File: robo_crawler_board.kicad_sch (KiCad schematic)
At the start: 24 parts, among them J1 Screw_Terminal_01x02, J2 Screw_Terminal_01x02, J3 Screw_Terminal_01x02, J4 Screw_Terminal_01x02, J5 Screw_Terminal_01x02, J6 Screw_Terminal_01x02, J7 Screw_Terminal_01x02, J8 Screw_Terminal_01x02, J9 Screw_Terminal_01x02, Q1 IRLZ44N, Q2 IRLZ44N, U1 DRV8871DDA, U2 DRV8871DDA, U3 DRV8871DDA, U4 DRV8871DDA, U8 DRV8871DDA, U9 DRV8871DDA

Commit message: cleaning repo
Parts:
- added R1, R2, R3, R4, R5, R6: 15k, Resistor_SMD:R_0805_2012Metric, symbol Device:R
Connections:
- net GND: now also R1.2, R2.2, R3.2, R4.2, R5.2, R6.2
- net at U1.4 (ILIM): now also R1.1
- net at U2.4 (ILIM): now also R2.1
- net at U4.4 (ILIM): now also R4.1
- net at U3.4 (ILIM): now also R3.1
- net at U9.4 (ILIM): now also R6.1
- net at U8.4 (ILIM): now also R5.1

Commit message: Reworking board design
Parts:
- removed J1, J2: Screw_Terminal_01x02, TerminalBlock:TerminalBlock_bornier-2_P5.08mm, symbol Connector:Screw_Terminal_01x02
- removed Q1, Q2: IRLZ44N, Package_TO_SOT_THT:TO-220-3_Vertical, symbol Transistor_FET:IRLZ44N
- removed U2, U3, U4: DRV8871DDA, Package_SO:Texas_HTSOP-8-1EP_3.9x4.9mm_P1.27mm_EP2.95x4.9mm_Mask2.4x3.1mm_ThermalVias, symbol Driver_Motor:DRV8871DDA
- added U5, U6, U7: DRV8871DDA, Package_SO:Texas_HTSOP-8-1EP_3.9x4.9mm_P1.27mm_EP2.95x4.9mm_Mask2.4x3.1mm_ThermalVias, symbol Driver_Motor:DRV8871DDA
- H1, H2, H3, H4: footprint MountingHole:MountingHole_2.2mm_M2 -> MountingHole:MountingHole_2.2mm_M2_Pad; symbol Mechanical:MountingHole -> Mechanical:MountingHole_Pad
- U2: renamed from U6; Part Name (none) -> LM2596 BC dev board
- renumbered J9 to J1, J8 to J2, U5 to U1, U7 to U3, U1 to U4
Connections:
- net +12V: now also U2.4 (OUT+), U5.5 (VM), U6.5 (VM), U7.5 (VM); no longer U3.4 (OUT+)
- net +5V: now also U3.4 (OUT+); no longer U2.4 (OUT+)
- net GND: now also H1.1, H2.1, H3.1, H4.1, U1.38 (GND), U5.1 (GND), U5.7 (GND), U5.9 (GND), U6.1 (GND), U6.7 (GND), U6.9 (GND), U7.1 (GND), U7.7 (GND), U7.9 (GND); no longer J1.1 (Pin_1), U1.15 (GND), U2.1 (IN-), U3.1 (IN-)
- net MOTOR1_CH2: now reaches U4.2 (IN2)
- net MOTOR1_CH2: now also U1.16 (IO13); no longer U1.12 (IO27)
- net MOTOR1_CH1: now reaches U4.3 (IN1)
- net MOTOR1_CH1: now also U1.14 (IO12); no longer U1.11 (IO26)
- net at J5.1 (Pin_1): now also U7.6 (OUT1)
- net at J5.2 (Pin_2): now also U7.8 (OUT2)
- net at J7.1 (Pin_1): now also U9.6 (OUT1)
- net at J7.2 (Pin_2): now also U9.8 (OUT2)
- net MOTOR5_CH2: now reaches U1.37 (IO23)
- net MOTOR5_CH2: now also U8.2 (IN2)
- net MOTOR5_CH1: now reaches U1.36 (IO22)
- net MOTOR5_CH1: now also U8.3 (IN1)
- net at R2.1: now also U5.4 (ILIM)
- net MOTOR2_CH1: now reaches U1.13 (IO14)
- net MOTOR2_CH1: now also U5.3 (IN1)
- net MOTOR2_CH2: now reaches U1.25 (IO0)
- net MOTOR2_CH2: now also U5.2 (IN2)
- net MOTOR3_CH1: now reaches U1.27 (IO16)
- net MOTOR3_CH1: now also U6.3 (IN1); no longer U9.3 (IN1)
- net MOTOR3_CH2: now reaches U1.28 (IO17)
- net MOTOR3_CH2: now also U6.2 (IN2); no longer U9.2 (IN2)
- net MOTOR4_CH1: now reaches U1.30 (IO18)
- net MOTOR4_CH1: now also U7.3 (IN1); no longer U8.3 (IN1)
- net MOTOR4_CH2: now reaches U1.31 (IO19)
- net MOTOR4_CH2: now also U7.2 (IN2); no longer U8.2 (IN2)
- net at R4.1: now also U7.4 (ILIM)
- net at J4.1 (Pin_1): now also U6.6 (OUT1); no longer U9.6 (OUT1)
- net at J4.2 (Pin_2): now also U6.8 (OUT2); no longer U9.8 (OUT2)
- net at U8.6 (OUT1): now also J6.1 (Pin_1); no longer J3.1 (Pin_1)
- net at U8.8 (OUT2): now also J6.2 (Pin_2); no longer J3.2 (Pin_2)
- net at R3.1: now also U6.4 (ILIM)
- net +Vin: no longer names the net of J1.2 (Pin_2), U2.2 (IN+), U3.2 (IN+)
- new net: J1.1 (Pin_1), U2.1 (IN-), U3.1 (IN-)
- new net: J3.1 (Pin_1), U5.6 (OUT1)
- new net: J3.2 (Pin_2), U5.8 (OUT2)
- new net MOTOR6_CH1: U1.11 (IO26), U9.3 (IN1)
- new net MOTOR6_CH2: U1.12 (IO27), U9.2 (IN2)
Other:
- moved on the sheet: J1, J2, R1, U2, U3, U4

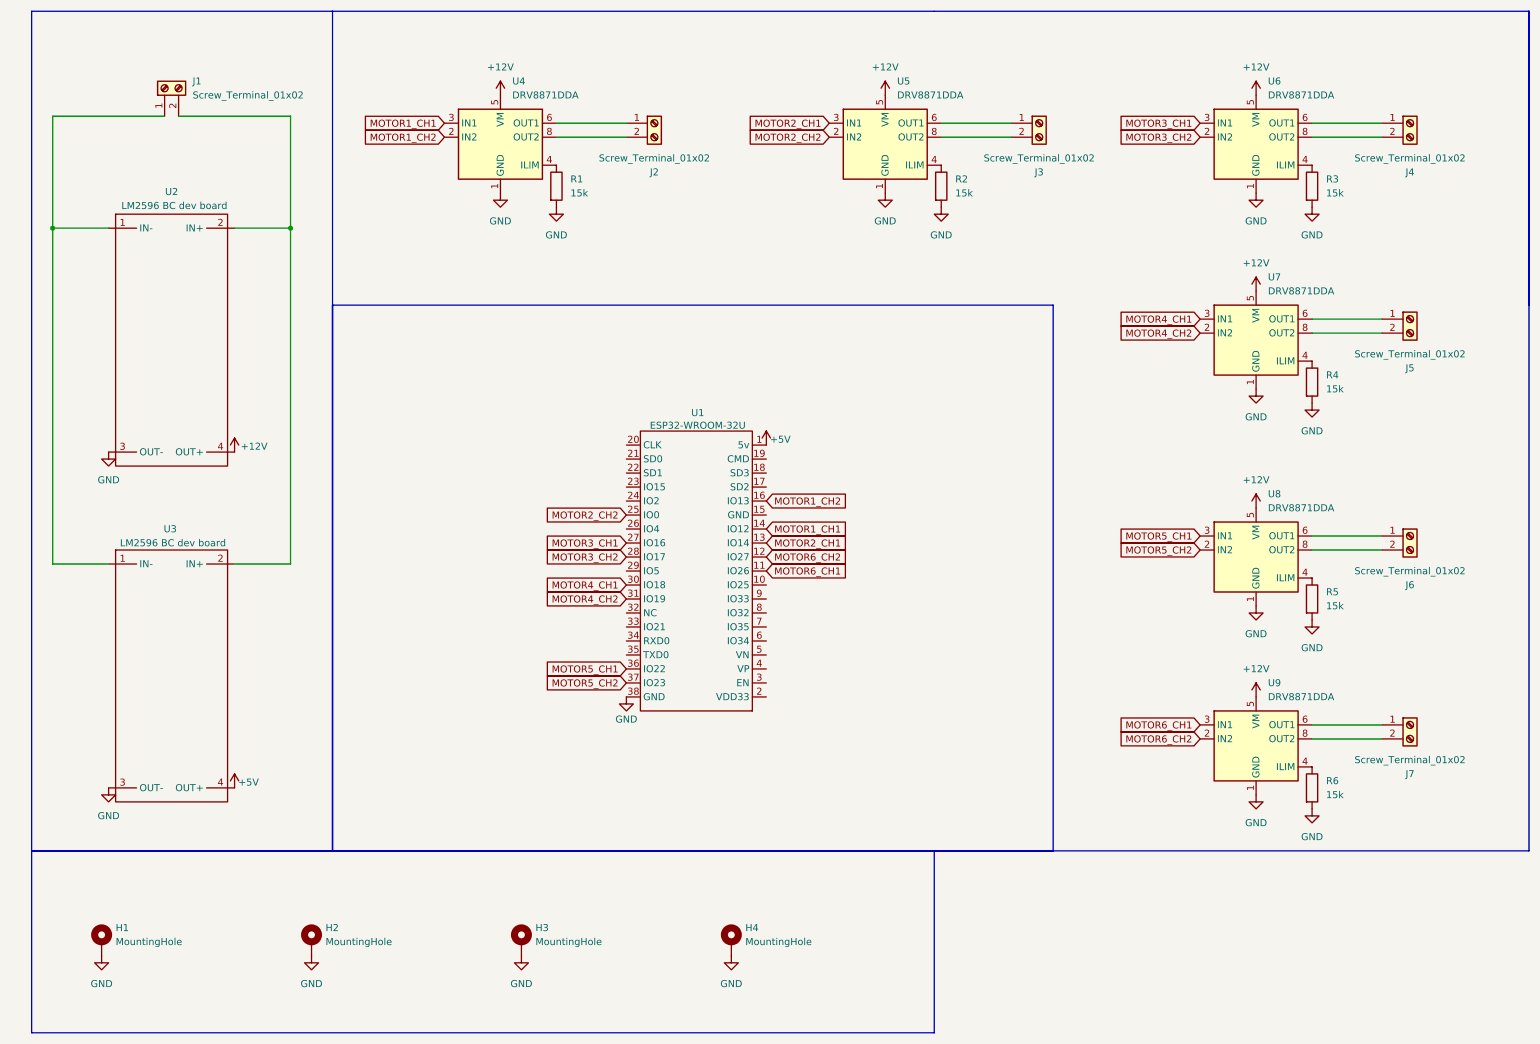
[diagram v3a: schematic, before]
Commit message: removed unnessesary controllers and adjusted layout
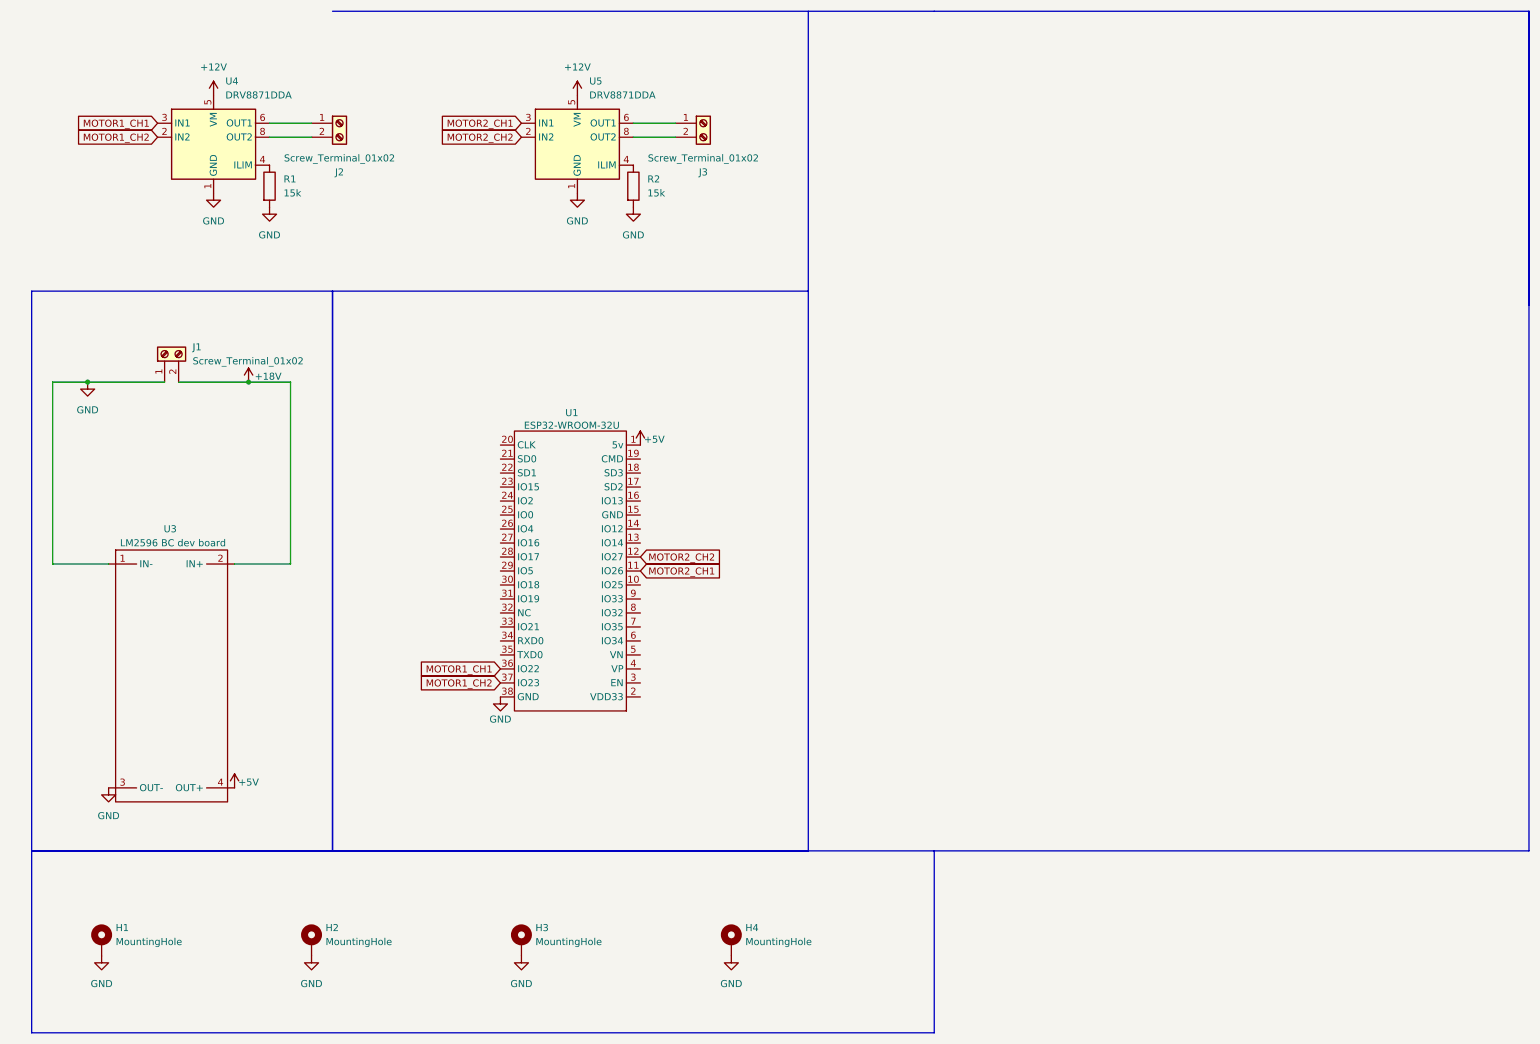
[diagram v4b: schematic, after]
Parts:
- removed J4, J5, J6, J7: Screw_Terminal_01x02, TerminalBlock:TerminalBlock_bornier-2_P5.08mm, symbol Connector:Screw_Terminal_01x02
- removed R3, R4, R5, R6: 15k, Resistor_SMD:R_0805_2012Metric, symbol Device:R
- removed U2: ~, deadzone_footprints:LM2596 DC-DC Buck Converter, symbol lm2596 dc-dc buck converter:LM2596 DC-DC Buck Converter
- removed U6, U7, U8, U9: DRV8871DDA, Package_SO:Texas_HTSOP-8-1EP_3.9x4.9mm_P1.27mm_EP2.95x4.9mm_Mask2.4x3.1mm_ThermalVias, symbol Driver_Motor:DRV8871DDA
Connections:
- net MOTOR5_CH1 is gone; now on net MOTOR1_CH1: U1.36 (IO22)
- net MOTOR5_CH2 is gone; now on net MOTOR1_CH2: U1.37 (IO23)
- net MOTOR6_CH1 is gone; now on net MOTOR2_CH1: U1.11 (IO26)
- net MOTOR6_CH2 is gone; now on net MOTOR2_CH2: U1.12 (IO27)
- net GND: now also J1.1 (Pin_1), U3.1 (IN-)
- net MOTOR1_CH1: no longer U1.14 (IO12)
- net MOTOR1_CH2: no longer U1.16 (IO13)
- net MOTOR2_CH1: no longer U1.13 (IO14)
- net MOTOR2_CH2: no longer U1.25 (IO0)
- net +18V: now reaches J1.2 (Pin_2), U3.2 (IN+)
- net MOTOR3_CH1: no longer names the net of U1.27 (IO16)
- net MOTOR3_CH2: no longer names the net of U1.28 (IO17)
- net MOTOR4_CH1: no longer names the net of U1.30 (IO18)
- net MOTOR4_CH2: no longer names the net of U1.31 (IO19)
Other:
- moved on the sheet: J1, J2, R1, U1, U4

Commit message: saving progress
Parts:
- added U2: DRV8262DDVR, DDV0044E-IPC_A, symbol DRV8262DDVR:DRV8262DDVR
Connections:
- net DRIVE_CH1: now reaches U1.30 (IO18)
- net DRIVE_CH2: now reaches U1.31 (IO19)
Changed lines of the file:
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@@
+		)
+	)
+	(global_label "DRIVE_CH1"
+		(shape input)
+		(at 97.79 116.84 180)
+		(fields_autoplaced yes)
+		(effects
+			(font
+				(size 1.27 1.27)
+			)
+			(justify right)
+		)
+		(property "Intersheetrefs" "${INTERSHEET_REFS}"
+			(at 84.6448 116.84 0)
+			(effects
+				(font
+					(size 1.27 1.27)
+				)
+				(justify right)
+				(hide yes)
+			)
+		)
+	)
+	(global_label "DRIVE_CH2"
+		(shape input)
+		(at 97.79 119.38 180)
+		(fields_autoplaced yes)
+		(effects
+			(font
+				(size 1.27 1.27)
+			)
+			(justify right)
+		)
+		(property "Intersheetrefs" "${INTERSHEET_REFS}"
+			(at 84.6448 119.38 0)
+			(effects
+				(font
+					(size 1.27 1.27)
+				)
+				(justify right)
+				(hide yes)
+			)
 		)
 	)
@@
 					(unit 1)
 				)
+			)
+		)
+	)
+	(symbol
+		(lib_id "DRV8262DDVR:DRV8262DDVR")
+		(at 189.23 46.99 0)
+		(unit 1)
+		(exclude_from_sim no)
+		(in_bom yes)
+		(on_board yes)
+		(dnp no)
+		(fields_autoplaced yes)
+		(property "Reference" "U2"
+			(at 217.17 36.83 0)
+			(effects
+				(font
+					(size 1.524 1.524)
+				)
+			)
+		)
+		(property "Value" "DRV8262DDVR"
+			(at 217.17 39.37 0)
+			(effects
+				(font
+					(size 1.524 1.524)
+				)
+			)
+		)
+		(property "Footprint" "DDV0044E-IPC_A"
+			(at 189.23 46.99 0)
+			(effects
+				(font
+					(size 1.27 1.27)
+					(italic yes)
+				)
+				(hide yes)
+			)
+		)
+		(property "Datasheet" "https://www.ti.com/lit/gpn/drv8262"
+			(at 189.23 46.99 0)
+			(effects
+				(font
+					(size 1.27 1.27)
+					(italic yes)
+				)
+				(hide yes)
+			)
+		)
+		(property "Description" ""
+			(at 189.23 46.99 0)
+			(effects
+				(font
+					(size 1.27 1.27)
+				)
+				(hide yes)
+			)
+		)
+		(pin "23"
+		)
+		(pin "22"
+		)
+		(pin "33"
+		)
+		(pin "11"
+		)
+		(pin "42"
+		)
+		(pin "38"
+		)
+		(pin "37"
+		)
+		(pin "2"
+		)
+		(pin "12"
+		)
+		(pin "21"
+		)
+		(pin "30"
+		)
+		(pin "34"
+		)
+		(pin "36"
+		)
+		(pin "35"
+		)
+		(pin "31"
+		)
+		(pin "43"
+		)
+		(pin "39"
+		)
+		(pin "32"
+		)
+		(pin "27"
+		)
+		(pin "26"
+		)
+		(pin "29"
+		)
+		(pin "25"
+		)
+		(pin "28"
+		)
+		(pin "20"
+		)
+		(pin "10"
+		)
+		(pin "17"
+		)
+		(pin "18"
+		)
+		(pin "13"
+		)
+		(pin "16"
+		)
+		(pin "6"
+		)
+		(pin "8"
+		)
+		(pin "9"
+		)
+		(pin "41"
+		)
+		(pin "1"
+		)
+		(pin "4"
+		)
+		(pin "19"
+		)
+		(pin "5"
+		)
+		(pin "40"
+		)
+		(pin "24"
+		)
+		(pin "15"
+		)
+		(pin "14"
+		)
+		(pin "7"
+		)
+		(pin "44"
+		)
+		(pin "3"
+		)
+		(instances
+			(project ""
+				(path "/8c23940b-1549-4d4e-a5eb-1280177a037e"
+					(reference "U2")
+					(unit 1)
+				)
